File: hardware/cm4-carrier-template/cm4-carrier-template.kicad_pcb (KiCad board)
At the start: 4 copper layers, 90 x 90 mm, 42 parts, among them J1 USB_C_Receptacle_USB2.0, J2 Micro_SD_Card, J3 Abracon_ARJM11-502, Q1 DMP2066LSN, SW1 BOOT, SW2 GLOBAL_EN, U5 Compute_Module_4_Functional, U6 TPD2EUSB30

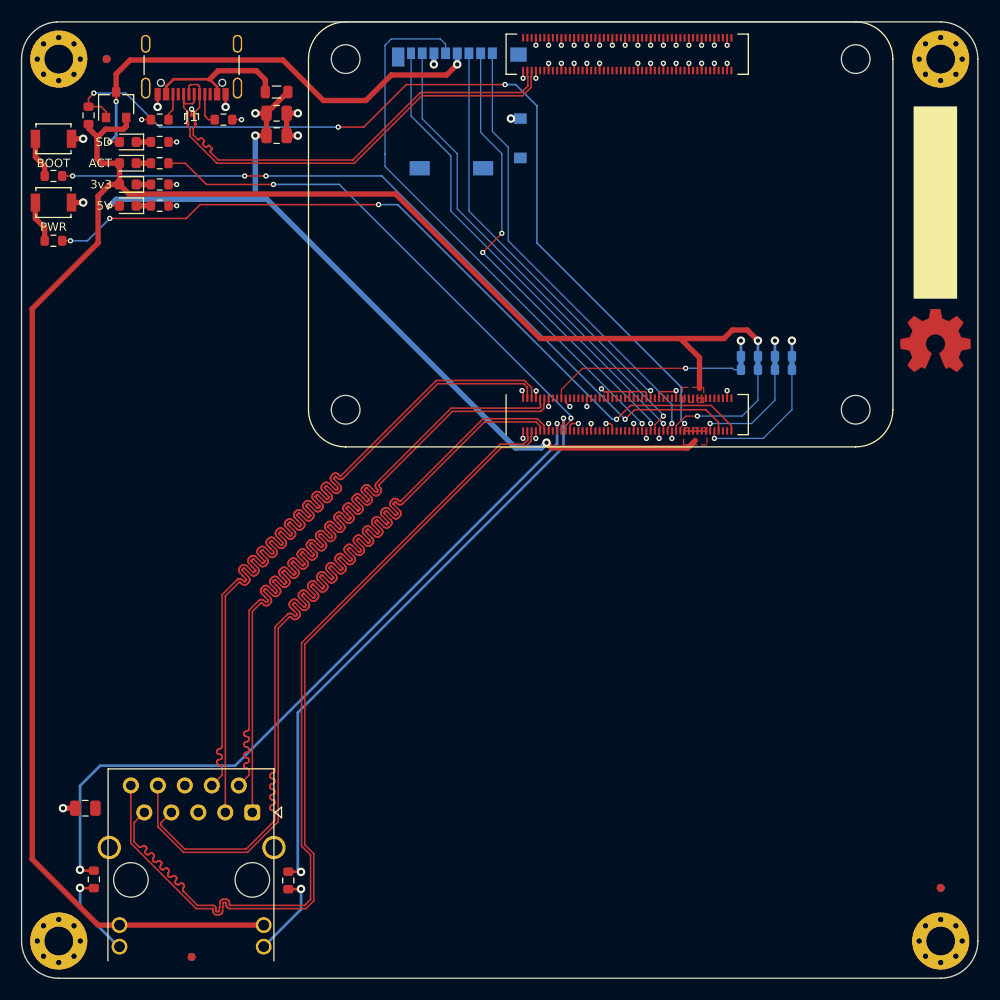
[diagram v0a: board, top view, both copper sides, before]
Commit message: Reworked cm4-carrier-template using latest cm4-carrier-net as base.
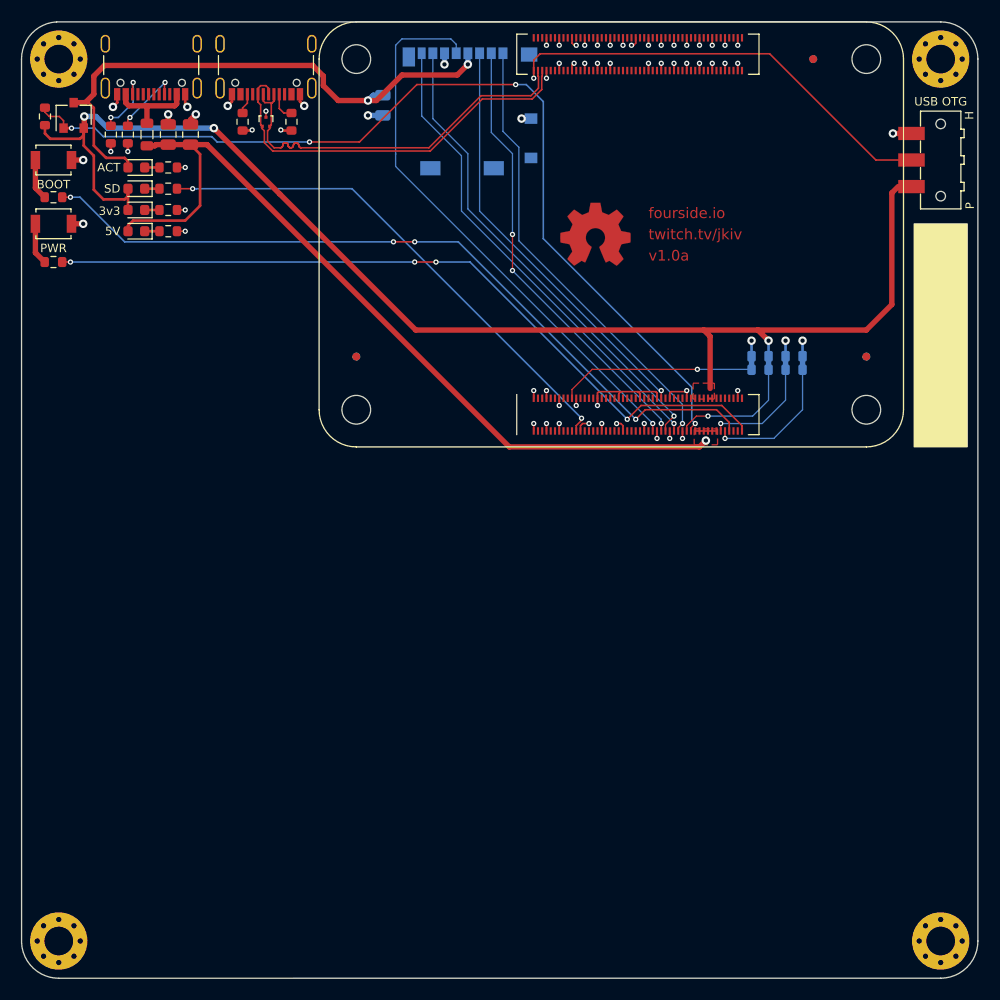
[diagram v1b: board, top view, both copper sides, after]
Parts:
- removed C3: 100n, Capacitor_SMD:C_0805_2012Metric
- added C4: 22u, Capacitor_SMD:C_0805_2012Metric, B.Cu at (114.0, 51.8)
- added SW3: USB_OTG, Button_Switch_SMD:SW_SPDT_CK-JS102011SAQN, F.Cu at (166.5, 57.0)
- J3: value Abracon_ARJM11-502 -> USB_C_Receptacle_USB2.0; footprint jkiv-library:RJ45_Abracon_ARJM11 -> jkiv-library:USB_C_Receptacle_GCT-USB4105
- R3, R4: value 220R -> 5k1
- moved R4 72.7 mm to (100.8, 53.4)
- moved R3 71.4 mm to (105.4, 53.4)
- moved J3 70.1 mm to (103.0, 48.3), turned to 180 degrees
- moved FID3 66.5 mm to (154.5, 47.5)
- moved FID6 66.5 mm to (154.5, 47.5)
- moved FID1 58.6 mm to (111.5, 75.5)
- moved FID4 58.6 mm to (111.5, 75.5)
- moved FID2 50.5 mm to (159.5, 75.5)
- moved FID5 50.5 mm to (159.5, 75.5)
- moved LOGO1 33.5 mm to (134.0, 64.0)
- moved FB1 12.8 mm to (91.8, 54.6), turned to 90 degrees
- moved C2 10.4 mm to (93.8, 54.6), turned to 90 degrees
- moved R1 9.11 mm to (90.0, 54.6), turned to 90 degrees
- moved C1 8.10 mm to (95.9, 54.6), turned to 90 degrees
- moved U6 7.00 mm to (103.0, 53.4)
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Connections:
- net /USB_VBUS renamed Net-(FB1-Pad2)
- J1 pad A6: /USB_D+ -> Net-(J1-PadA6)
- J1 pad A7: /USB_D- -> Net-(J1-PadA7)
- J1 pad B6: /USB_D+ -> Net-(J1-PadB6)
- J1 pad B7: /USB_D- -> Net-(J1-PadB7)
- J1 pad S1: Net-(J1-PadS1) -> GND
- R3 pad 1: Net-(J3-Pad14) -> GND
- R3 pad 2: /~E0_LEDR -> Net-(J3-PadA5)
- R4 pad 1: Net-(J3-Pad12) -> GND
- R4 pad 2: /~E0_LEDL -> Net-(J3-PadB5)
- U5 pad 10: /E0_TR0- -> (no net)
- U5 pad 101: GND -> /USB_OTG_ID
- U5 pad 11: /E0_TR2+ -> (no net)
- U5 pad 12: /E0_TR0+ -> (no net)
- U5 pad 15: /E0_LEDL -> (no net)
- U5 pad 16: Net-(U5-Pad16) -> (no net)
- U5 pad 17: /~E0_LEDL -> (no net)
- U5 pad 18: Net-(U5-Pad18) -> (no net)
- U5 pad 19: /~E0_LEDR -> (no net)
- U5 pad 3: /E0_TR3+ -> (no net)
- U5 pad 4: /E0_TR1+ -> (no net)
- U5 pad 5: /E0_TR3- -> (no net)
- U5 pad 6: /E0_TR1- -> (no net)
- U5 pad 9: /E0_TR2- -> (no net)
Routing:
- net /E0_TR2+: track 95.2 -> 0.00 mm
- net /E0_TR2-: track 95.1 -> 0.00 mm
- net /E0_TR0-: track 82.1 -> 0.00 mm
- net /E0_TR3+: track 82.1 -> 0.00 mm
- net /E0_TR1+: track 82.1 -> 0.00 mm
- net /E0_TR1-: track 82.1 -> 0.00 mm
- net /E0_TR0+: track 82.1 -> 0.00 mm
- net /E0_TR3-: track 82.0 -> 0.00 mm
- net /~E0_LEDL: track 70.1 -> 0.00 mm, vias 2 -> 0
- net /~E0_LEDR: track 55.7 -> 0.00 mm, vias 2 -> 0
- net +3V3: track 177.9 -> 124.5 mm, vias 1 -> 3
- net /USB_OTG_ID: track 0.00 -> 41.6 mm, vias 0 -> 1
- net /SD_PWR: track 44.2 -> 54.5 mm, vias 3 -> 2
- net Net-(J3-Pad12): track 8.43 -> 0.00 mm, vias 1 -> 0
- net Net-(J3-Pad14): track 8.10 -> 0.00 mm, vias 1 -> 0
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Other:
- board text added: "H"
- board text added: "P"
- board text added: "USB OTG"
- board text added: "fourside.io"
- board text added: "twitch.tv/jkiv"
- board text added: "v1.0a"
